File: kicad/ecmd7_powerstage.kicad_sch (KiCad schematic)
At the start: 57 parts, among them Q1 IRFS3806, Q11 MMBT3904, Q12 MMBT3904, Q2 IRFS3806, Q3 IRFS3806, Q4 IRFS3806, Q5 IRFS3806, Q6 IRFS3806, U1 TMC6200-TA

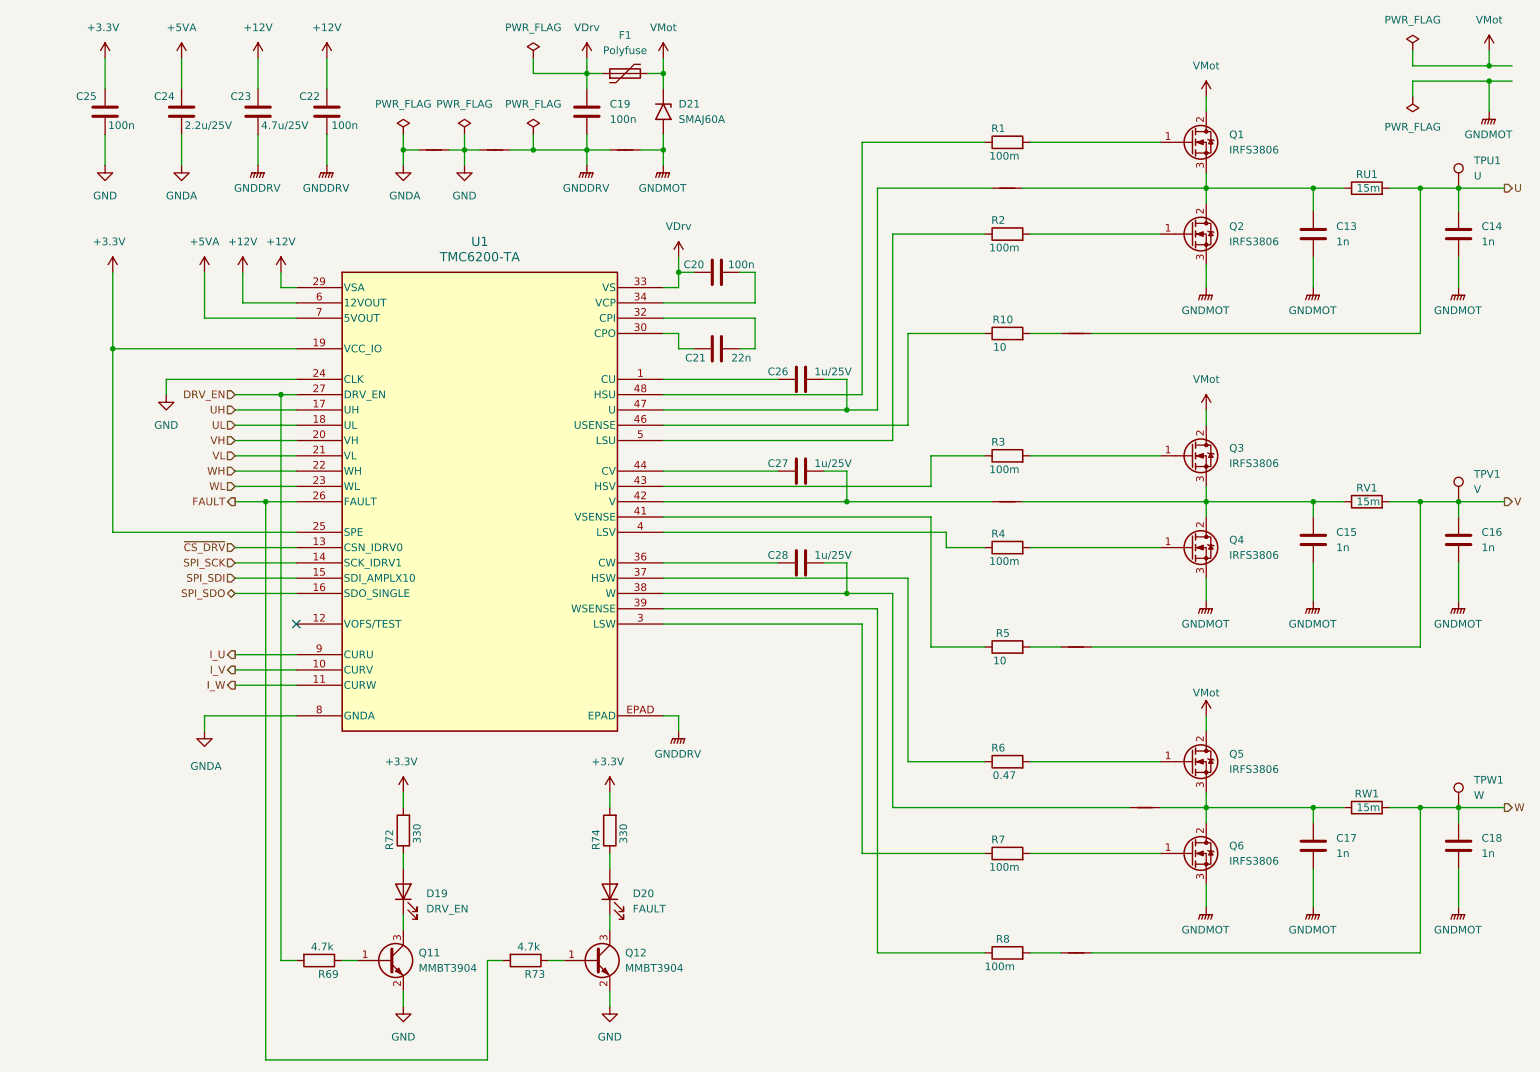
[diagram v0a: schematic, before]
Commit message: Cleanup schematic, add busses
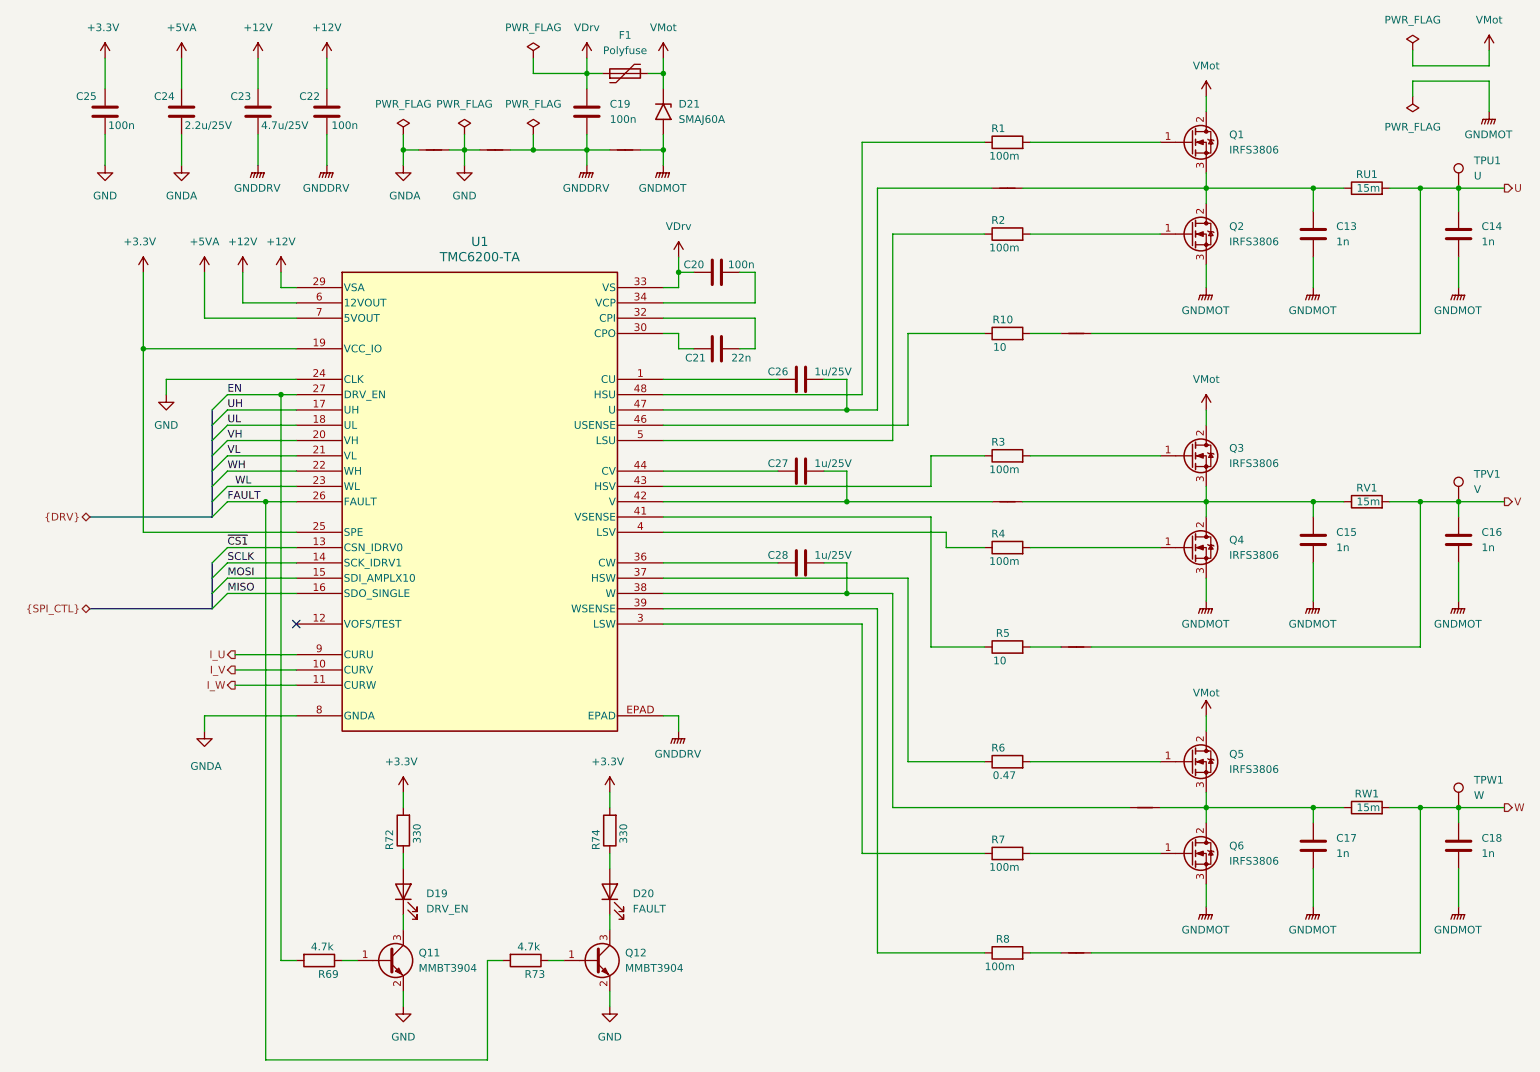
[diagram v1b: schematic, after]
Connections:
- net DRV_EN renamed EN
- net SPI_SCK renamed SCLK
- net SPI_SDI renamed MOSI
- net SPI_SDO renamed MISO
- net ~{CS_DRV} renamed ~{CS1}
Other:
- title: (none) -> ECMD7 Power Stage

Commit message: General schematic cleanup
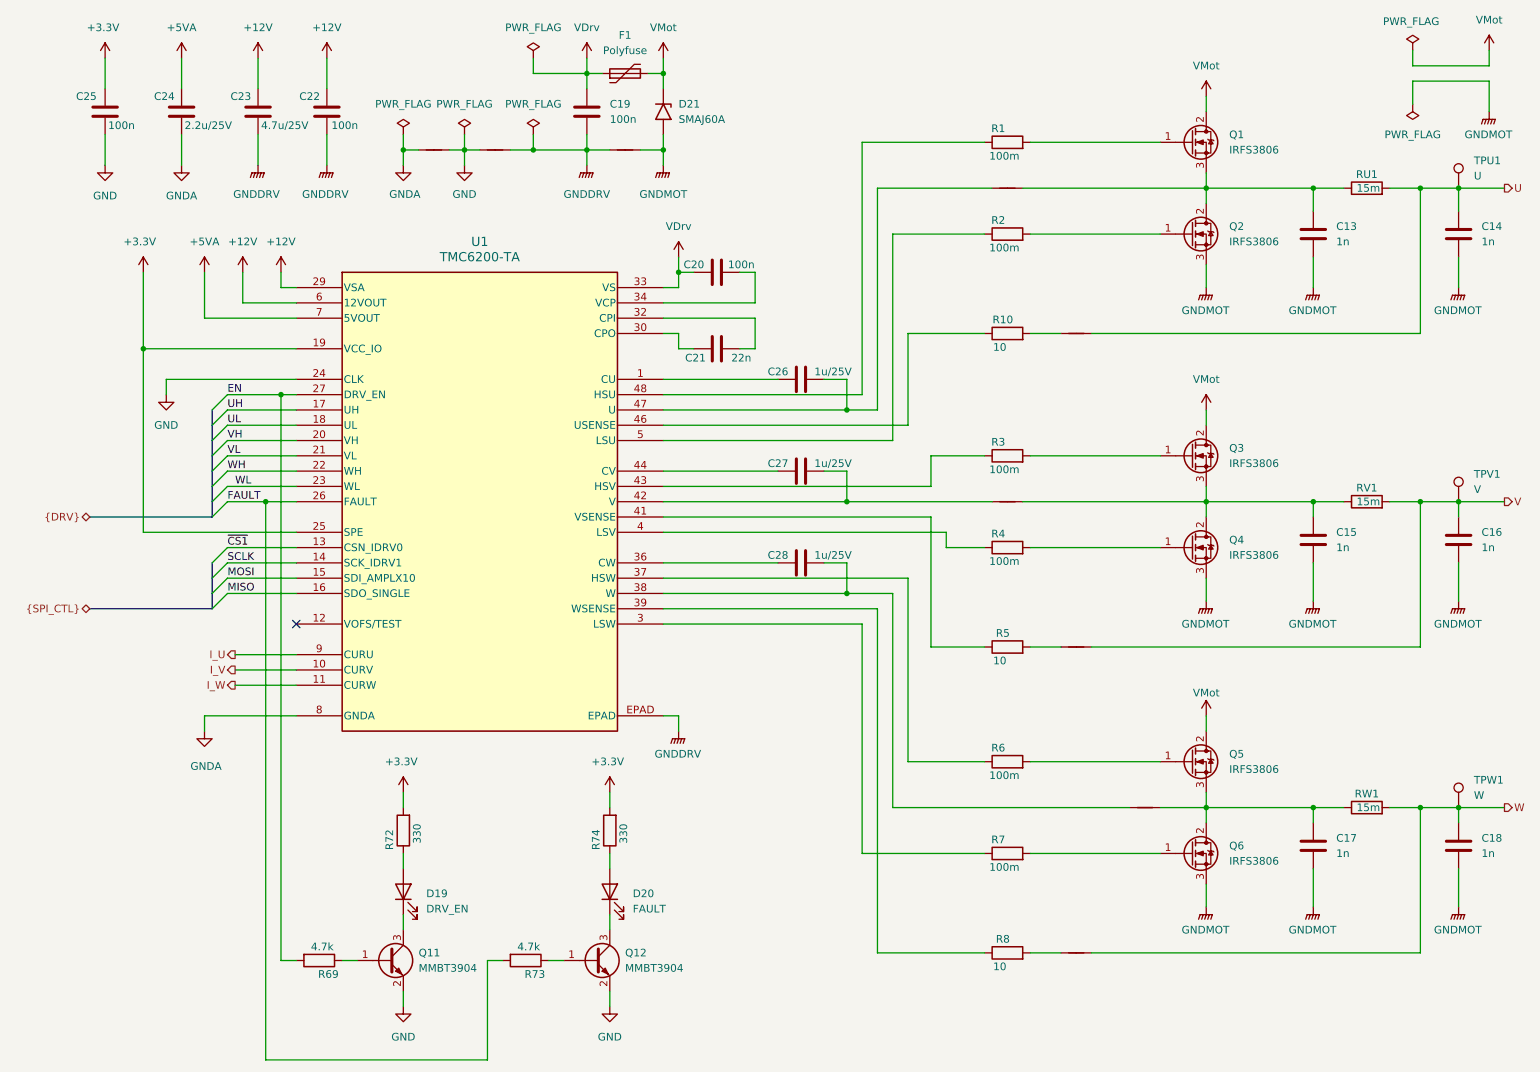
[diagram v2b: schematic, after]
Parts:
- R6: value 0.47 -> 100m
- R8: value 100m -> 10
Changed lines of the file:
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@@
 	(wire
 		(pts
-			(xy 304.8 68.58) (xy 304.8 66.04)
+			(xy 304.8 69.85) (xy 304.8 66.04)
 		)
 		(stroke
@@
 		(on_board yes)
 		(dnp no)
-		(fields_autoplaced yes)
 		(property "Reference" "#FLG01"
 			(at 304.8 59.055 0)
@@
 		)
 		(property "Value" "PWR_FLAG"
-			(at 304.8 55.88 0)
+			(at 304.546 56.134 0)
 			(effects
 				(font
@@
 		(on_board yes)
 		(dnp no)
-		(fields_autoplaced yes)
 		(property "Reference" "#PWR0218"
 			(at 167.64 85.09 0)
@@
 		)
 		(property "Value" "GNDDRV"
-			(at 167.513 83.82 0)
+			(at 167.64 84.836 0)
 			(effects
 				(font
@@
 			)
 		)
-		(property "Value" "100m"
+		(property "Value" "10"
 			(at 236.22 213.106 90)
 			(effects
@@
 		(on_board yes)
 		(dnp no)
-		(fields_autoplaced yes)
 		(property "Reference" "#PWR035"
 			(at 147.32 86.36 0)
@@
 		)
 		(property "Value" "GND"
-			(at 147.32 85.09 0)
+			(at 147.32 84.836 0)
 			(effects
 				(font
@@
 		(on_board yes)
 		(dnp no)
-		(fields_autoplaced yes)
 		(property "Reference" "#PWR0148"
 			(at 180.34 85.09 0)
@@
 		)
 		(property "Value" "GNDMOT"
-			(at 180.213 83.82 0)
+			(at 180.34 84.836 0)
 			(effects
 				(font
@@
 		)
 		(property "Value" "GNDA"
-			(at 137.414 85.09 0)
+			(at 137.414 84.836 0)
 			(effects
 				(font
@@
 			)
 		)
-		(property "Value" "0.47"
+		(property "Value" "100m"
 			(at 236.982 181.356 90)
 			(effects
@@
 		(on_board yes)
 		(dnp no)
-		(fields_autoplaced yes)
 		(property "Reference" "#PWR037"
 			(at 113.03 85.09 0)
@@
 		)
 		(property "Value" "GNDDRV"
-			(at 112.903 83.82 0)
+			(at 112.776 84.836 0)
 			(effects
 				(font
@@
 		(on_board yes)
 		(dnp no)
-		(fields_autoplaced yes)
 		(property "Reference" "#PWR010"
 			(at 124.46 85.09 0)
@@
 		)
 		(property "Value" "GNDDRV"
-			(at 124.333 83.82 0)
+			(at 124.206 84.836 0)
 			(effects
 				(font
@@
 	(symbol
 		(lib_id "power:PWR_FLAG")
-		(at 304.8 68.58 180)
+		(at 304.8 69.85 180)
 		(unit 1)
 		(exclude_from_sim no)
@@
 		(fields_autoplaced yes)
 		(property "Reference" "#FLG07"
-			(at 304.8 70.485 0)
+			(at 304.8 71.755 0)
 			(effects
 				(font
@@
 		)
 		(property "Value" "PWR_FLAG"
-			(at 304.8 73.66 0)
+			(at 304.8 74.93 0)
 			(effects
 				(font
@@
 		)
 		(property "Footprint" ""
-			(at 304.8 68.58 0)
+			(at 304.8 69.85 0)
 			(effects
 				(font
@@
 		)
 		(property "Datasheet" "~"
-			(at 304.8 68.58 0)
+			(at 304.8 69.85 0)
 			(effects
 				(font
@@
 		)
 		(property "Description" "Special symbol for telling ERC where power comes from"
-			(at 304.8 68.58 0)
+			(at 304.8 69.85 0)
 			(effects
 				(font
